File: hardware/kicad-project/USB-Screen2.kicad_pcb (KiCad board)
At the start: 2 copper layers, 32 x 34 mm, 22 parts, among them J1 USB_B_Micro, J2 Conn_01x04, J3 USB_C_Receptacle_USB2.0, K1 SW_4*4mm, K2 SW_4*4mm, K3 SW_4*4mm, Q1 NPN, U1 ZJY154T-PG04, U2 CH551, U3 SC662

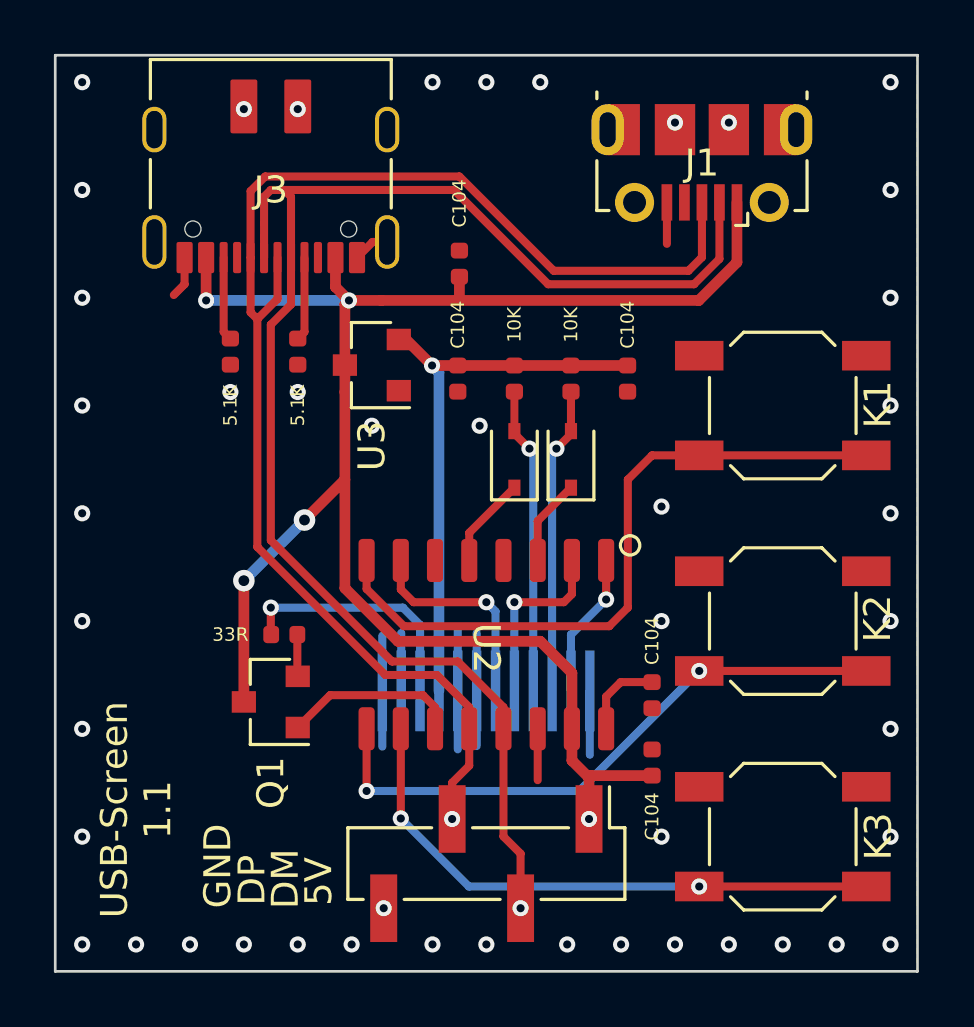
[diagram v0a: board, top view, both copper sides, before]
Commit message: 改0402封装为0603封装,对手工焊接更友好.
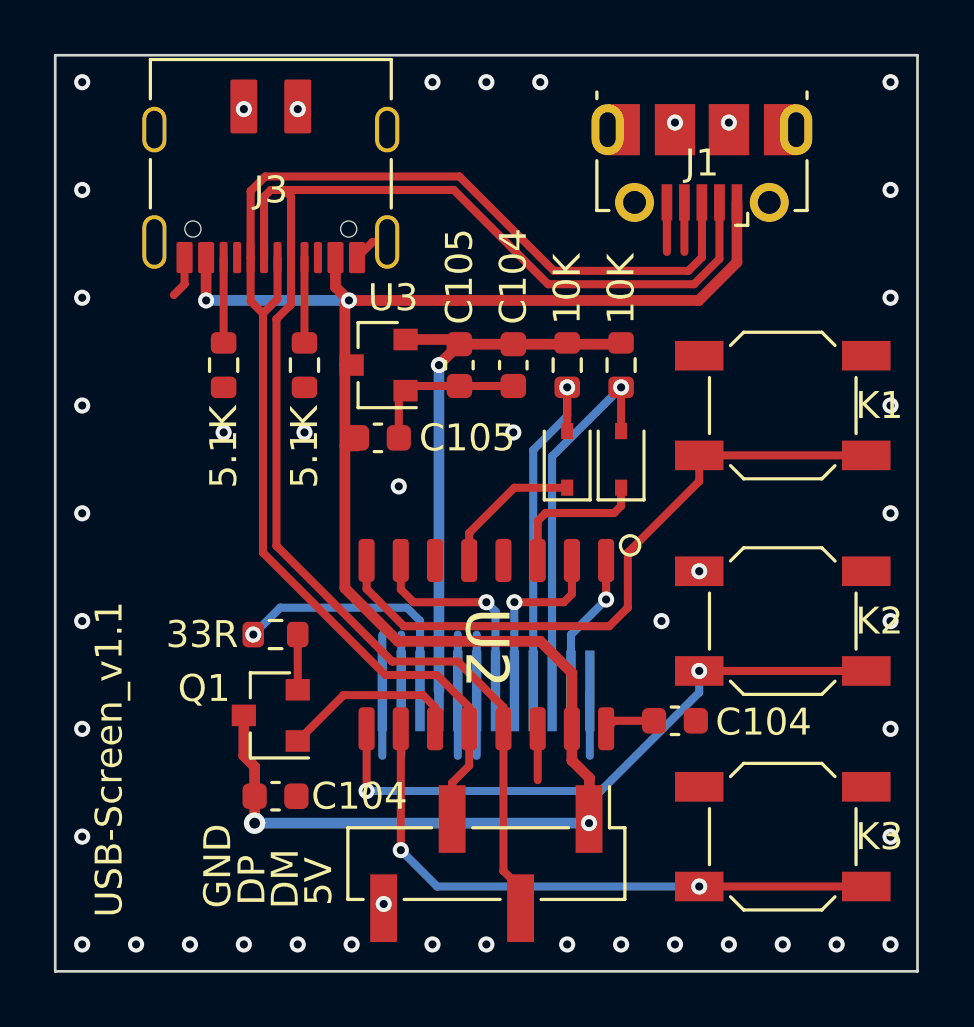
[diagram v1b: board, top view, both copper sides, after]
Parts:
- C1, C2, C3, C4, C5: footprint Capacitor_SMD:C_0402_1005Metric -> Capacitor_SMD:C_0603_1608Metric
- R1, R2, R6, R7, R8: footprint Resistor_SMD:R_0402_1005Metric -> Resistor_SMD:R_0603_1608Metric
- moved C5 20.9 mm to (92.2, 110.5), turned to 0 degrees
- moved C2 15.8 mm to (96.0, 97.2), turned to 0 degrees
- moved C4 6.26 mm to (99.0, 94.5)
- moved C1 2.12 mm to (101.0, 94.5)
- moved R2 2.02 mm to (103.0, 94.5)
- moved D5 1.96 mm to (103.0, 98.0)
- moved R1 1.93 mm to (105.0, 94.5)
- moved D4 1.86 mm to (105.0, 98.0)
- moved C3 1.27 mm to (107.0, 107.7), turned to 180 degrees
- moved R7 0.56 mm to (93.2, 94.5)
- moved R8 0.56 mm to (90.2, 94.5)
- moved Q1 0.50 mm to (92.0, 107.5)
- moved R6 0.33 mm to (92.2, 104.5)
- moved U3 0.25 mm to (96.0, 94.5)
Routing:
- net GND: track 25.7 -> 33.0 mm, vias 46 -> 45
- net +5V: track 64.9 -> 69.5 mm, vias 5 -> 4
- net /SDA: track 11.4 -> 14.0 mm
- net Net-(D4-Pad1): track 3.21 -> 5.47 mm
- net /SCL: track 11.4 -> 13.4 mm
- net Net-(D5-Pad1): track 3.39 -> 5.35 mm
- net Net-(J1-Pad4): track 0.00 -> 1.84 mm
- net Net-(C3-Pad2): track 3.12 -> 1.90 mm
- net /K1: track 25.6 -> 24.6 mm
- net /K3: track 21.6 -> 22.3 mm
- net /USB_D+: track 51.3 -> 51.0 mm, vias 1 -> 0
- net /USB_D-: track 55.5 -> 55.4 mm, vias 1 -> 0
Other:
- board text added: "USB-Screen_v1.1"
- board text removed: "USB-Screen 1.1"
